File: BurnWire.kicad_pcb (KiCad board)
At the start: 2 copper layers, 14 parts, among them J1 B6B-XH-A_LF__SN_, U1 ADP2303ARDZ

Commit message: done
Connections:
- U1 pad 9: unconnected-(U1-PADGND-Pad9) -> GND
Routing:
- net GND: track 118.4 -> 120.5 mm
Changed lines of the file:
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@@
 			(psa4output no)
 			(plot_black_and_white yes)
-			(sketchpadsonfab no)
+			(sketchpadsonfab yes)
 			(plotpadnumbers no)
 			(hidednponfab no)
 			(sketchdnponfab yes)
 			(crossoutdnponfab yes)
-			(subtractmaskfromsilk no)
+			(subtractmaskfromsilk yes)
 			(outputformat 1)
 			(mirror no)
-			(drillshape 1)
+			(drillshape 0)
 			(scaleselection 1)
-			(outputdirectory "")
+			(outputdirectory "gerber/")
 		)
 	)
@@
 	(net 9 "Net-(U1-FB)")
 	(net 10 "unconnected-(U1-NC-Pad6)")
-	(net 11 "unconnected-(U1-PADGND-Pad9)")
 	(footprint "TestPoint:TestPoint_2Pads_Pitch5.08mm_Drill1.3mm"
 		(layer "F.Cu")
@@
 			(property pad_prop_heatsink)
 			(layers "F.Cu" "F.Mask")
-			(net 11 "unconnected-(U1-PADGND-Pad9)")
+			(net 3 "GND")
 			(pinfunction "PADGND")
 			(pintype "power_in")
@@
 	)
 	(segment
-		(start 155.951 89.549)
-		(end 162.9743 89.549)
+		(start 160.5 103.5)
+		(end 160.5 103)
 		(width 0.2)
 		(layer "F.Cu")
@@
 	)
 	(segment
-		(start 160.5 103.5)
-		(end 160.5 103)
+		(start 160.1375 99.1375)
+		(end 159.699999 99.575)
 		(width 0.2)
 		(layer "F.Cu")
@@
 	)
 	(segment
-		(start 160.1375 99.1375)
-		(end 159.699999 99.575)
+		(start 162.9743 89.549)
+		(end 165.049 91.6237)
 		(width 0.2)
 		(layer "F.Cu")
@@
 	)
 	(segment
-		(start 154.35 91.15)
-		(end 155.951 89.549)
-		(width 0.2)
-		(layer "F.Cu")
-		(net 1)
-	)
-	(segment
-		(start 162.9743 89.549)
-		(end 165.049 91.6237)
-		(width 0.2)
-		(layer "F.Cu")
-		(net 1)
-	)
-	(segment
 		(start 157.63525 108)
 		(end 158.515 107.12025)
@@
 	)
 	(segment
+		(start 154.35 91.15)
+		(end 155.951 89.549)
+		(width 0.2)
+		(layer "F.Cu")
+		(net 1)
+	)
+	(segment
 		(start 159.8875 99.3875)
 		(end 158.9925 99.3875)
@@
 	)
 	(segment
+		(start 155.951 89.549)
+		(end 162.9743 89.549)
+		(width 0.2)
+		(layer "F.Cu")
+		(net 1)
+	)
+	(segment
 		(start 162.5 94.1727)
 		(end 162.5 96.774999)
@@
 	)
 	(segment
+		(start 157.015002 101.25)
+		(end 158.120002 100.145)
+		(width 0.2)
+		(layer "F.Cu")
+		(net 3)
+	)
+	(segment
 		(start 168.7574 91.6237)
 		(end 169.7474 90.6337)
@@
 		(width 0.2)
 		(layer "F.Cu")
+		(net 3)
+	)
+	(segment
+		(start 156.475 101.25)
+		(end 157.015002 101.25)
+		(width 0.2)
+		(layer "F.Cu")

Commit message: Add design rules to layout
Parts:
- removed J1: B6B-XH-A_LF__SN_, imported_footprints:JST_B6B-XH-A_LF__SN_
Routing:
- net Net-(U1-PGOOD): track 47.9 -> 0.00 mm, vias 1 -> 0
- net /Vout: track 73.0 -> 29.9 mm
- net /EN: track 21.7 -> 0.00 mm, vias 2 -> 0
- net /VBatt: track 55.9 -> 36.3 mm, vias 6 -> 4
- net /VCutN: track 37.0 -> 19.7 mm, vias 4 -> 2
- net GND: track 120.5 -> 107.4 mm
- net Net-(U1-SW): track 42.9 -> 42.4 mm

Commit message: reworked most of the layout
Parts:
- added J1: B6B-XH-A_LF__SN_, imported_footprints:JST_B6B-XH-A_LF__SN_, F.Cu at (162.1, 80.2)
- moved C4 18.3 mm to (146.4, 80.7)
- moved C3 18.3 mm to (137.4, 80.7)
- moved R3 18.2 mm to (154.8, 86.1)
- moved C5 17.4 mm to (142.6, 90.2)
- moved L1 17.3 mm to (157.1, 90.7)
- moved C2 16.8 mm to (134.6, 108.5)
- moved C1 15.5 mm to (134.7, 100.5)
- moved R2 14.0 mm to (165.7, 86.2)
- moved TP2 12.5 mm to (166.3, 99.5)
- moved TP1 6.76 mm to (154.6, 97.9)
- moved U1 5.38 mm to (157.6, 106.5)
- moved R1 5.29 mm to (167.3, 106.8)
- moved CR1 2.29 mm to (168.7, 93.1)
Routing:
- net GND: track 107.4 -> 137.8 mm, vias 4 -> 0
- net Net-(U1-BST): track 25.0 -> 0.00 mm, vias 2 -> 0
- net (no net): track 0.00 -> 15.0 mm
- net /VCutN: track 19.7 -> 32.2 mm, vias 2 -> 4
- net Net-(U1-SW): track 42.4 -> 31.8 mm
- net /Vout: track 29.9 -> 38.7 mm
- net Net-(U1-PGOOD): track 0.00 -> 6.03 mm
- net Net-(U1-FB): track 4.90 -> 0.00 mm, vias 2 -> 0
- net /VBatt: track 36.3 -> 34.5 mm, vias 4 -> 0

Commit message: finished routing
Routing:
- net /VBatt: track 34.5 -> 115.2 mm, vias 0 -> 2
- net /EN: track 0.00 -> 48.0 mm, vias 0 -> 2
- net Net-(U1-PGOOD): track 6.03 -> 39.1 mm, vias 0 -> 2
- net Net-(U1-BST): track 0.00 -> 22.2 mm
- net GND: track 137.8 -> 157.3 mm
- net Net-(U1-FB): track 0.00 -> 7.82 mm
- net (no net): track 15.0 -> 17.3 mm
- net Net-(U1-SW): track 31.8 -> 33.3 mm
- net /VCutN: track 32.2 -> 30.7 mm

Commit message: burnwire design complete
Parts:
- moved C2 1.01 mm to (133.6, 108.1)
- moved C5 1.01 mm to (141.6, 89.8)
- moved J1 1.01 mm to (161.1, 79.8)
- moved L1 1.01 mm to (156.1, 90.3)
- moved TP1 1.01 mm to (153.7, 97.5)
- moved CR1 1.01 mm to (167.7, 92.8)
- moved U1 1.01 mm to (156.7, 106.2)
- moved C1 1.01 mm to (133.8, 100.1)
- moved C3 1.01 mm to (136.5, 80.3)
- moved C4 1.01 mm to (145.5, 80.3)
- moved R2 1.01 mm to (164.8, 85.8)
- moved R1 1.01 mm to (166.3, 106.5)
- moved R3 1.01 mm to (153.9, 85.8)
- moved TP2 1.01 mm to (165.3, 99.2)
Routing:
- net /VCutN: track 30.7 -> 31.2 mm
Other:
- board outline added: 49.9 x 44.1 mm

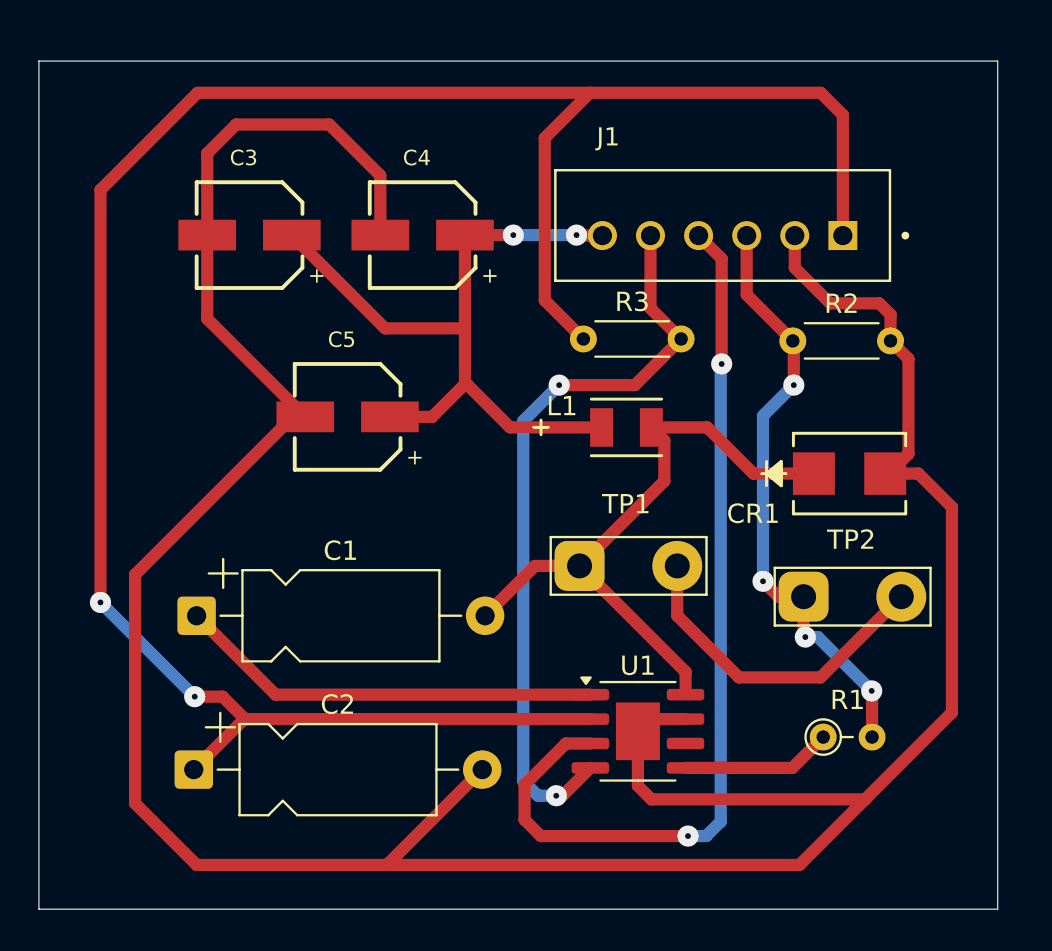
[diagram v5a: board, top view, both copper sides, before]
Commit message: reduced number of vias
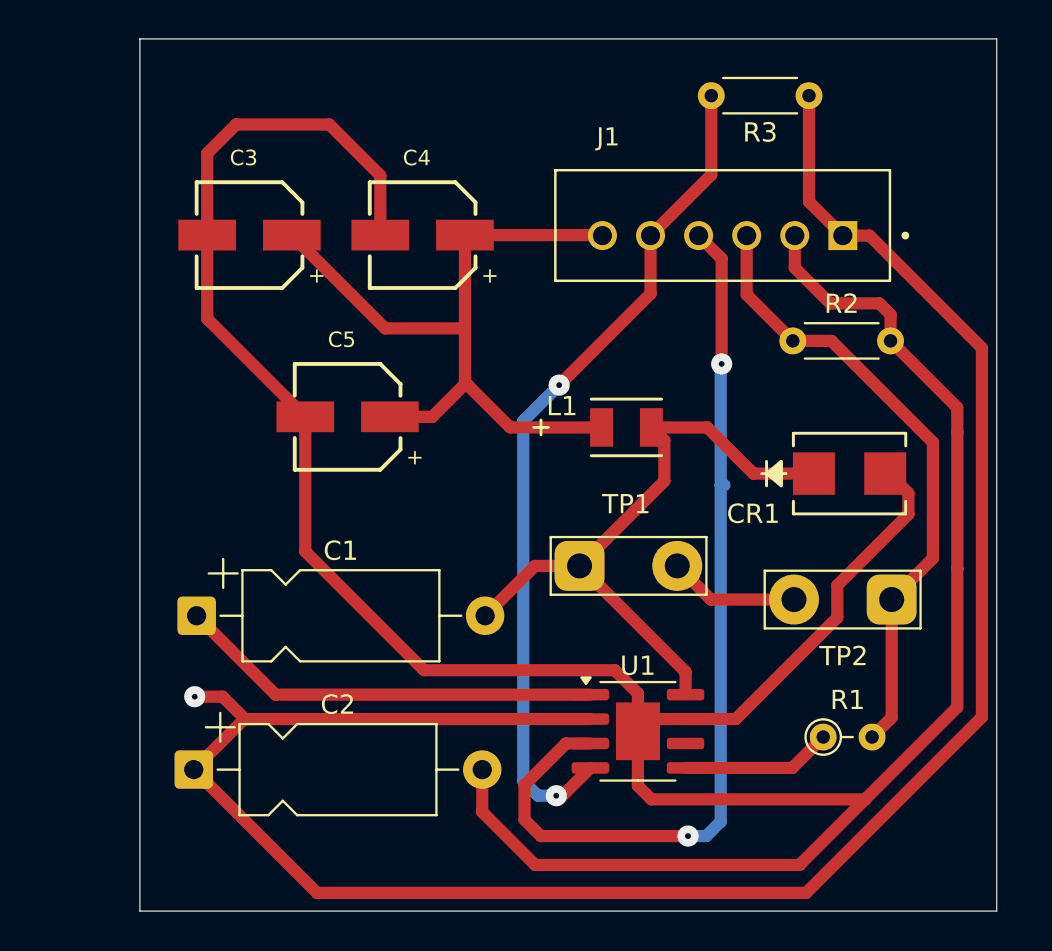
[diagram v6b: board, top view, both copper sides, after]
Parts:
- moved R3 17.3 mm to (165.6, 73.1), turned to 180 degrees
- moved TP2 4.58 mm to (169.9, 99.3), turned to 180 degrees
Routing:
- net (no net): track 17.3 -> 6.79 mm
- net /VBatt: track 115.2 -> 109.1 mm, vias 2 -> 1
- net Net-(U1-PGOOD): track 39.1 -> 44.1 mm
- net /VCutN: track 31.2 -> 32.6 mm, vias 4 -> 0
- net GND: track 157.3 -> 158.0 mm
- net /Vout: track 38.5 -> 38.6 mm, vias 2 -> 0
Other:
- board size 49.9 x 44.1 mm -> 44.5 x 45.3 mm

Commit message: fixed some DRC violations
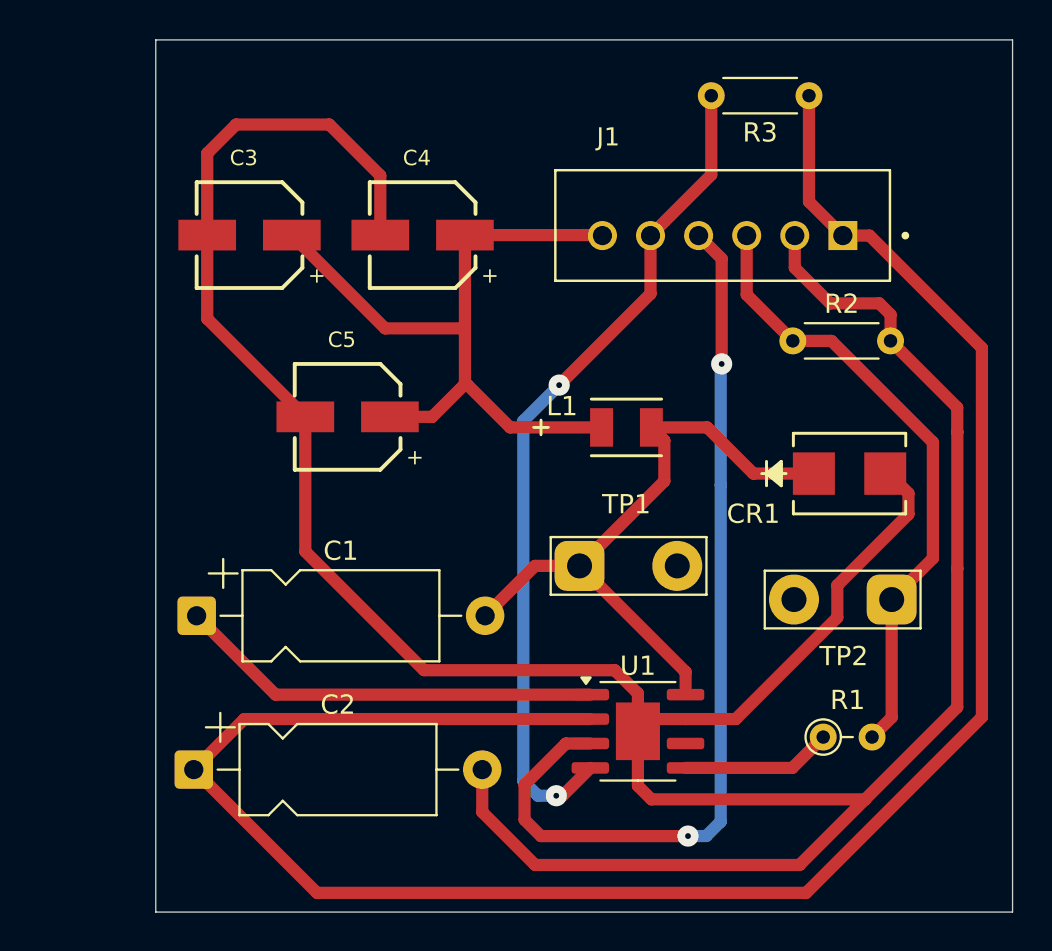
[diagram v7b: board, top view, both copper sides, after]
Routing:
- net (no net): track 6.79 -> 0.00 mm
- net /VBatt: track 109.1 -> 106.0 mm, vias 1 -> 0
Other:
- board size 44.5 x 45.3 mm -> 44.6 x 45.3 mm
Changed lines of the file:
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@@
 	)
 	(gr_rect
-		(start 130.8 70.15)
-		(end 175.35 115.5)
+		(start 131.625 70.2)
+		(end 176.175 115.55)
 		(stroke
 			(width 0.05)
@@
 	)
 	(segment
-		(start 158.74 97.55)
-		(end 160.49 99.3)
-		(width 0.635)
-		(layer "F.Cu")
-		(net 0)
-	)
-	(segment
-		(start 160.49 99.3)
-		(end 164.81 99.3)
-		(width 0.635)
-		(layer "F.Cu")
-		(net 0)
-	)
-	(segment
 		(start 151.3425 97.55)
 		(end 148.75 100.1425)
@@
 	)
 	(segment
-		(start 135.1 104.35)
-		(end 136.2275 105.4775)
-		(width 0.635)
-		(layer "F.Cu")
-		(net 4)
-	)
-	(segment
 		(start 133.6 108.1425)
 		(end 136.2275 105.515)
@@
 	)
 	(segment
-		(start 136.2275 105.4775)
-		(end 136.2275 105.515)
-		(width 0.635)
-		(layer "F.Cu")
-		(net 4)
-	)
-	(segment
-		(start 133.65 104.35)
-		(end 135.1 104.35)
-		(width 0.635)
-		(layer "F.Cu")
-		(net 4)
-	)
-	(segment
 		(start 140.0075 114.55)
 		(end 133.6 108.1425)
@@
 		(width 0.635)
 		(layer "F.Cu")
-		(net 4)
-	)
-	(via
-		(at 133.65 104.35)
-		(size 1.1)
-		(drill 0.3)
-		(layers "F.Cu" "B.Cu")
 		(net 4)
 	)
@@
 	)
 	(segment
-		(start 161 93.35)
-		(end 161.2 93.35)
+		(start 160.2525 111.5975)
+		(end 159.3 111.5975)
 		(width 0.635)
 		(layer "B.Cu")
@@
 	)
 	(segment
-		(start 159.3 111.5975)
+		(start 161 110.85)
 		(end 160.2525 111.5975)
 		(width 0.635)
@@
 		(width 0.635)
 		(layer "B.Cu")
-		(net 6)
-	)
-	(segment
-		(start 160.2525 111.5975)
-		(end 161 110.85)
-		(width 0.635)
-		(layer "B.Cu")

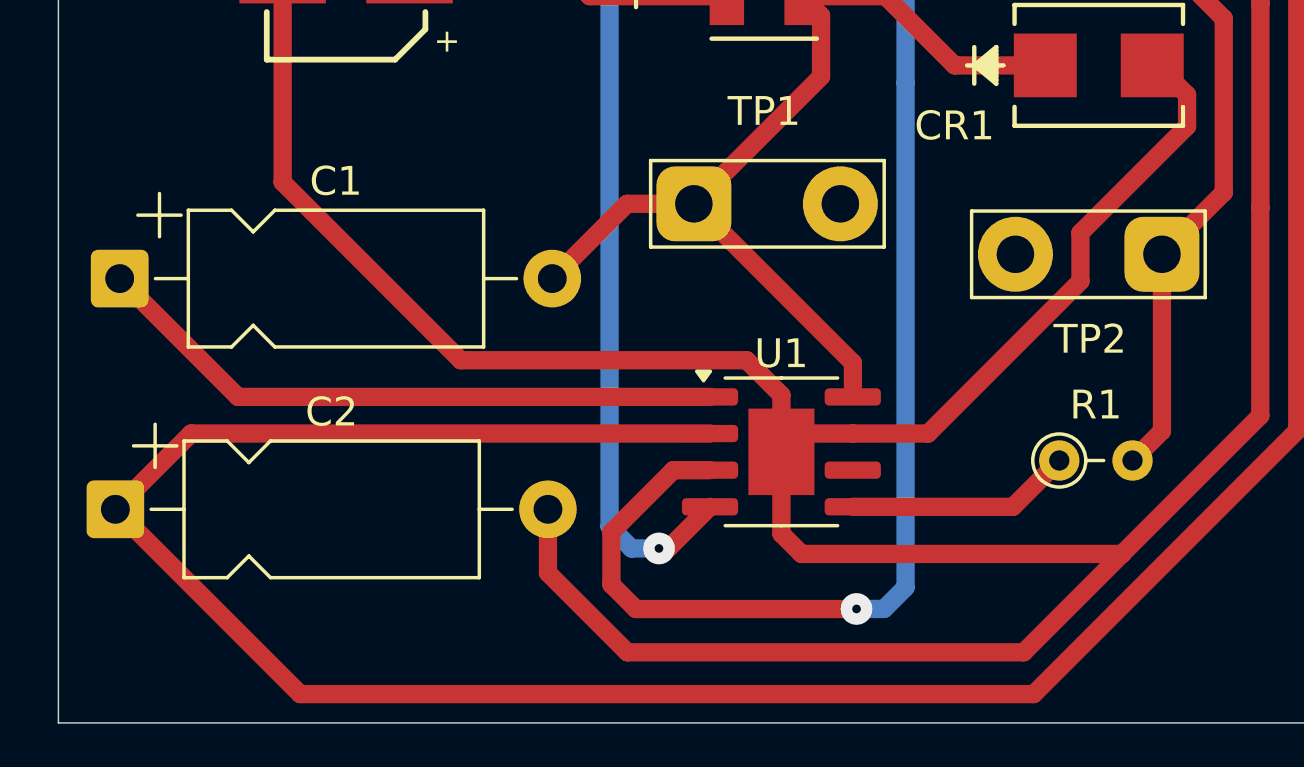
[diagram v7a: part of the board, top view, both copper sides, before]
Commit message: unflipped version; passes DRC
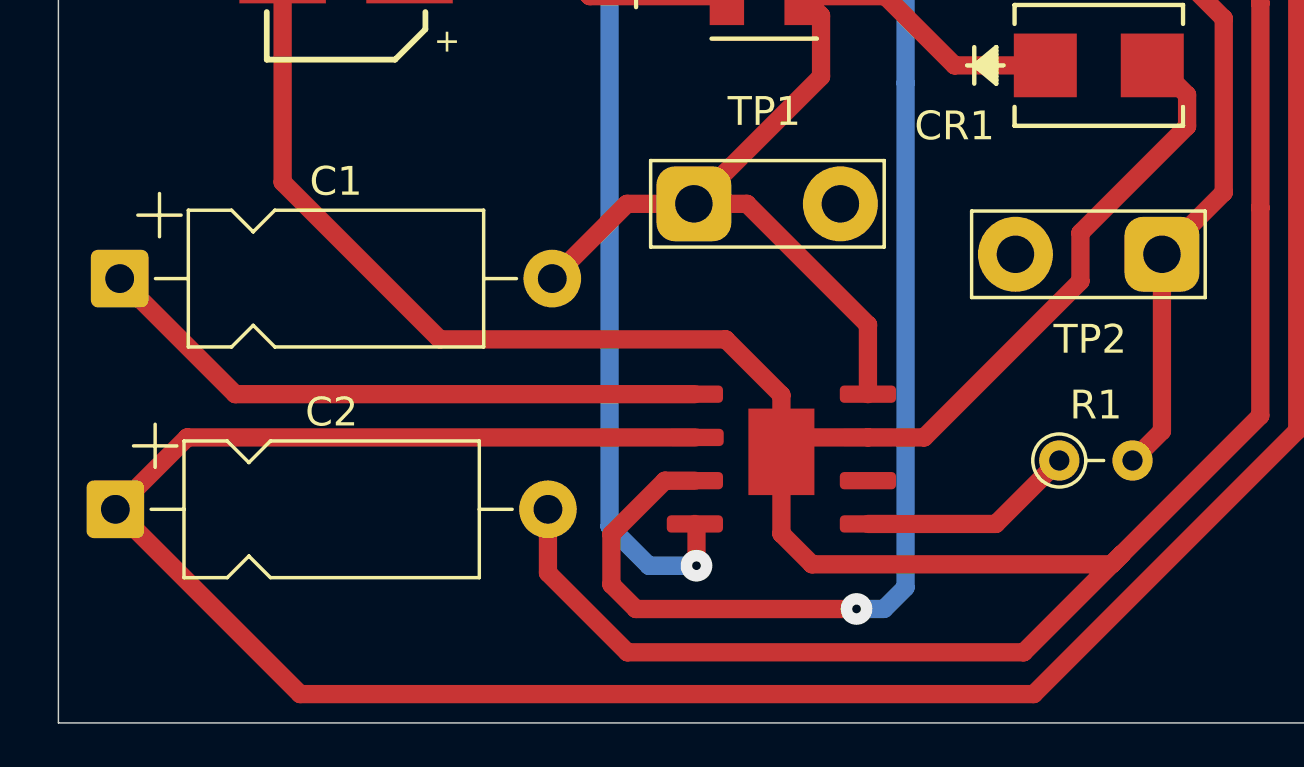
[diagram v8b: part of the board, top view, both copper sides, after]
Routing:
- net Net-(U1-SW): track 33.3 -> 34.9 mm
- net GND: track 158.0 -> 159.1 mm
- net /EN: track 48.0 -> 47.2 mm
- net Net-(U1-PGOOD): track 44.1 -> 44.7 mm
- net Net-(U1-BST): track 22.2 -> 21.6 mm
- net /VBatt: track 106.0 -> 105.4 mm
